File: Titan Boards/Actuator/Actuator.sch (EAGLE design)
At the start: 82 parts, among them Q1 MOSFET-NCH-AO3404A, Q12 MOSFET-NCH-AO3404A, Q13 MOSFET-NCH-AO3404A, Q14 MOSFET-NCH-AO3404A, Q15 MOSFET-NCH-AO3404A, Q17 MOSFET-NCH-AO3404A, Q18 FDD4141TO252, Q2 MOSFET-NCH-AO3404A, Q3 MOSFET-NCH-AO3404A, Q4 MOSFET-NCH-AO3404A, Q5 MOSFET-NCH-AO3404A, Q6 FDD4141TO252, Y1 16MHz, Y3 32.768kHz

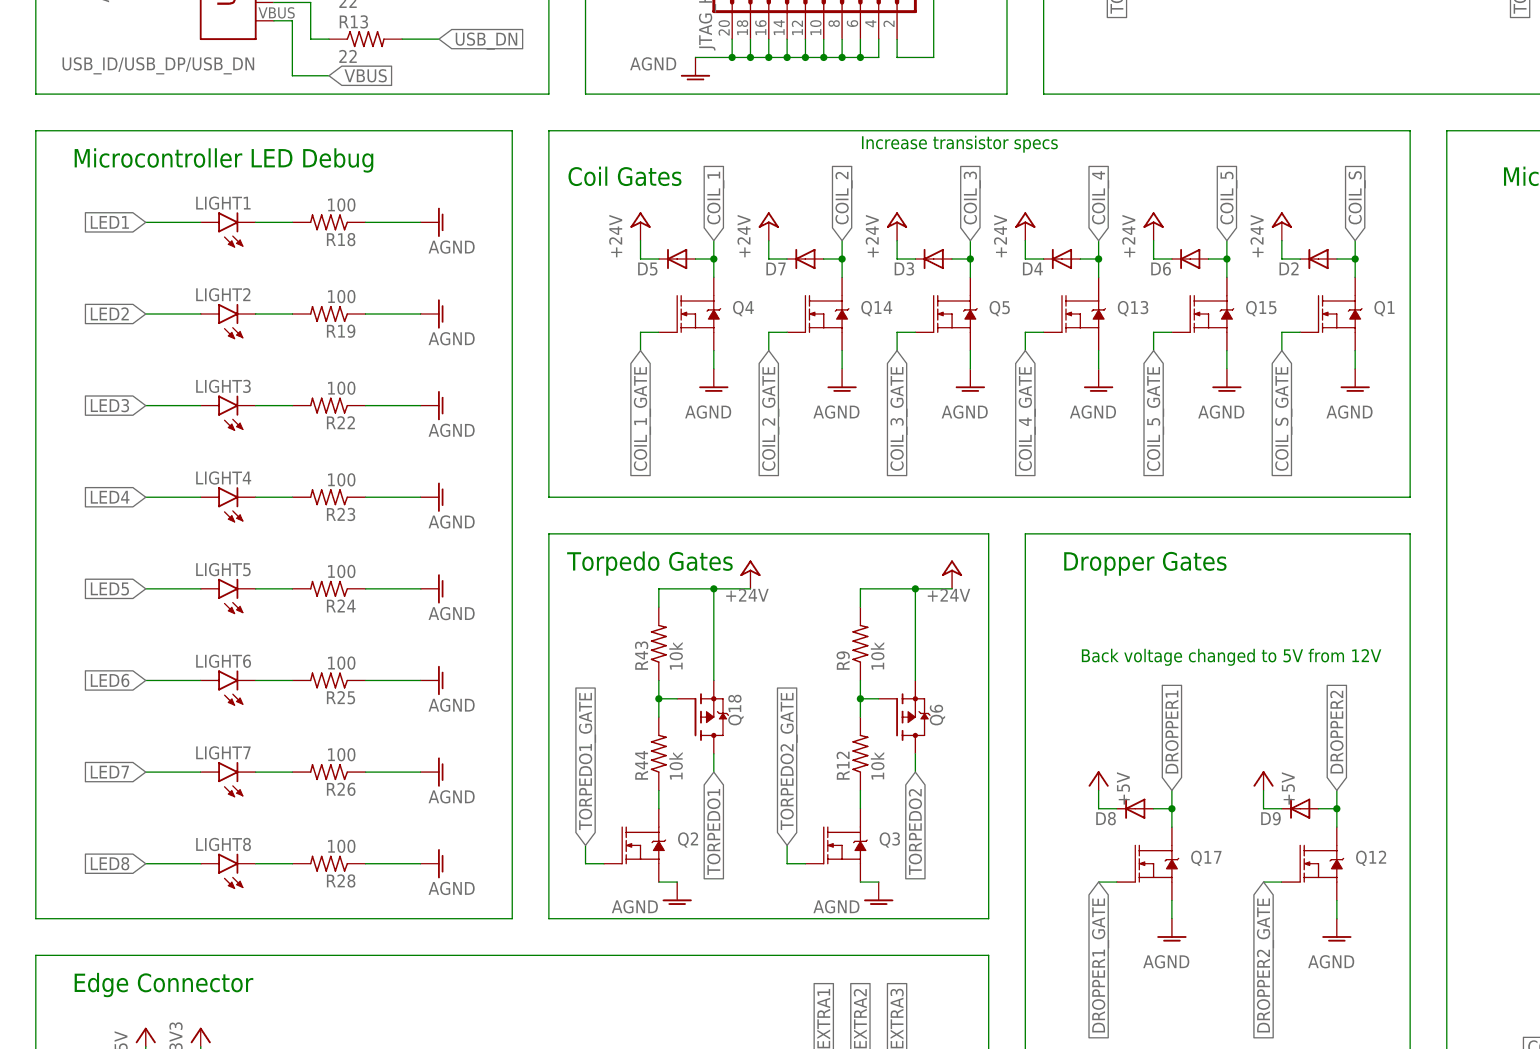
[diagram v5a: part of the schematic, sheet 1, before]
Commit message: Actuator double MOSFET addition
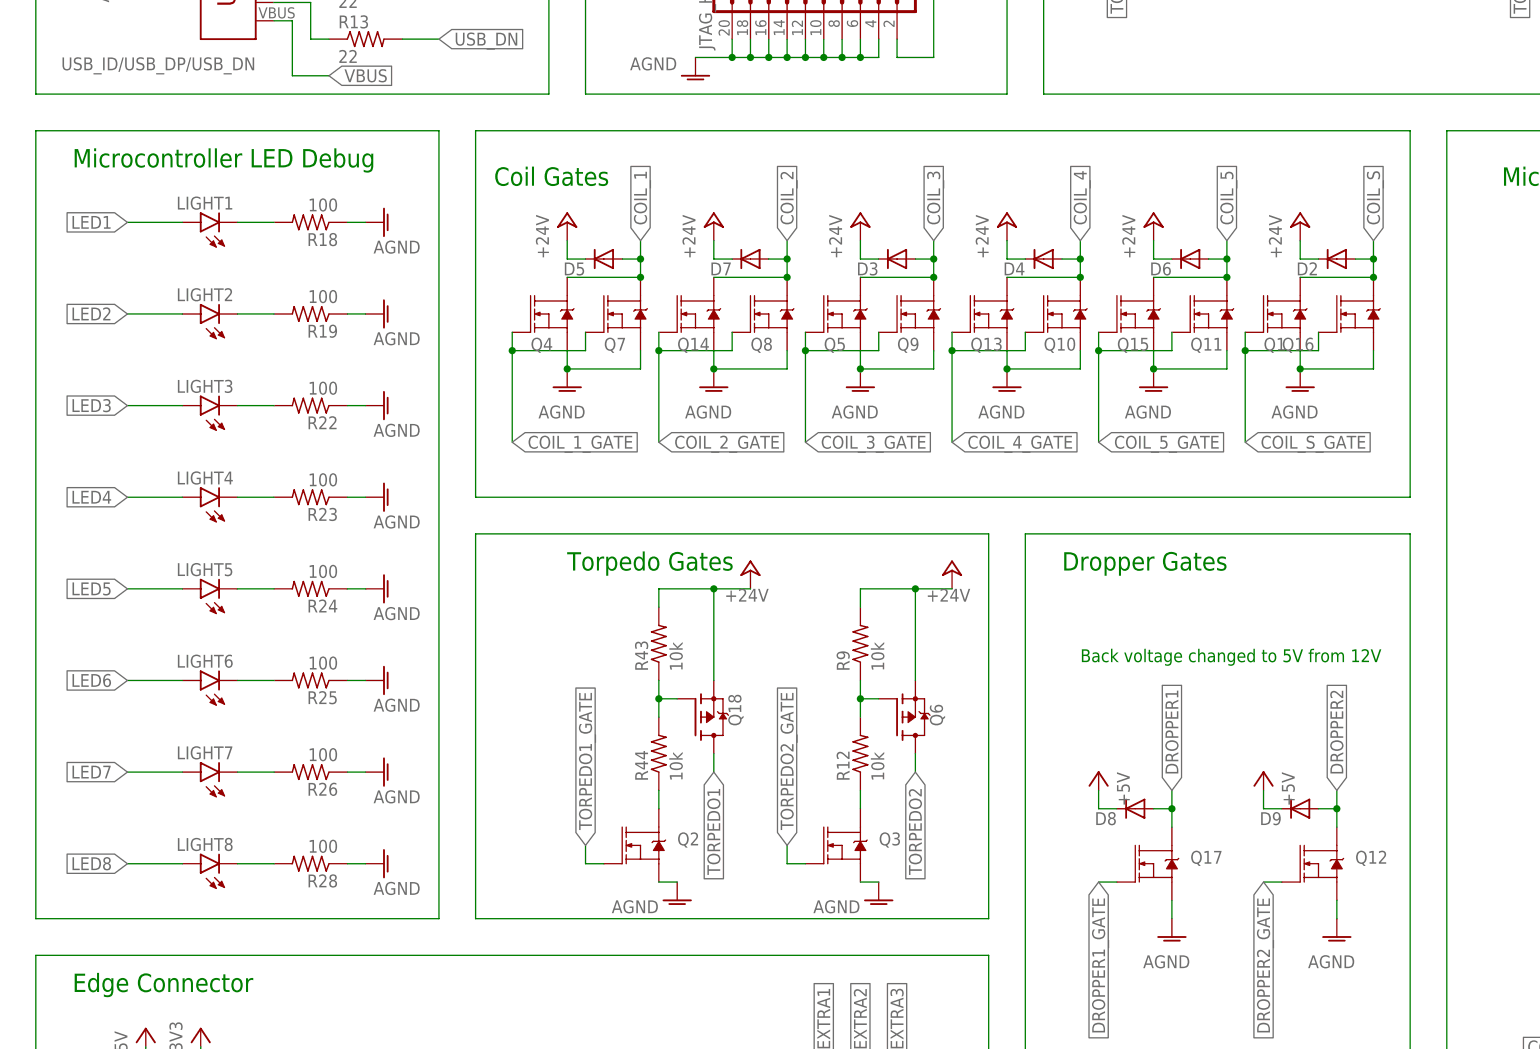
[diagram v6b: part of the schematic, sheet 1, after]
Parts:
- added Q10, Q11, Q16, Q7, Q8, Q9: MOSFET-NCH-AO3404A, SparkFun-DiscreteSemi:MOSFET-NCH-AO3404A
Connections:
- removed net AGND1: Q15.S
- net AGND: now also Q10.S, Q11.S, Q15.S, Q16.S, Q7.S, Q8.S, Q9.S
- net COIL_1: now also Q7.D
- net COIL_1_GATE: now also Q7.G
- net COIL_2: now also Q8.D
- net COIL_2_GATE: now also Q8.G
- net COIL_3: now also Q9.D
- net COIL_3_GATE: now also Q9.G
- net COIL_4: now also Q10.D
- net COIL_4_GATE: now also Q10.G
- net COIL_5: now also Q11.D
- net COIL_5_GATE: now also Q11.G
- net COIL_S: now also Q16.D
- net COIL_S_GATE: now also Q16.G
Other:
- note removed: "Increase transistor specs"
- moved on the sheet: D2, D3, D4, D5, D7, LIGHT1, LIGHT2, LIGHT3, LIGHT4, LIGHT5, LIGHT6, LIGHT7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

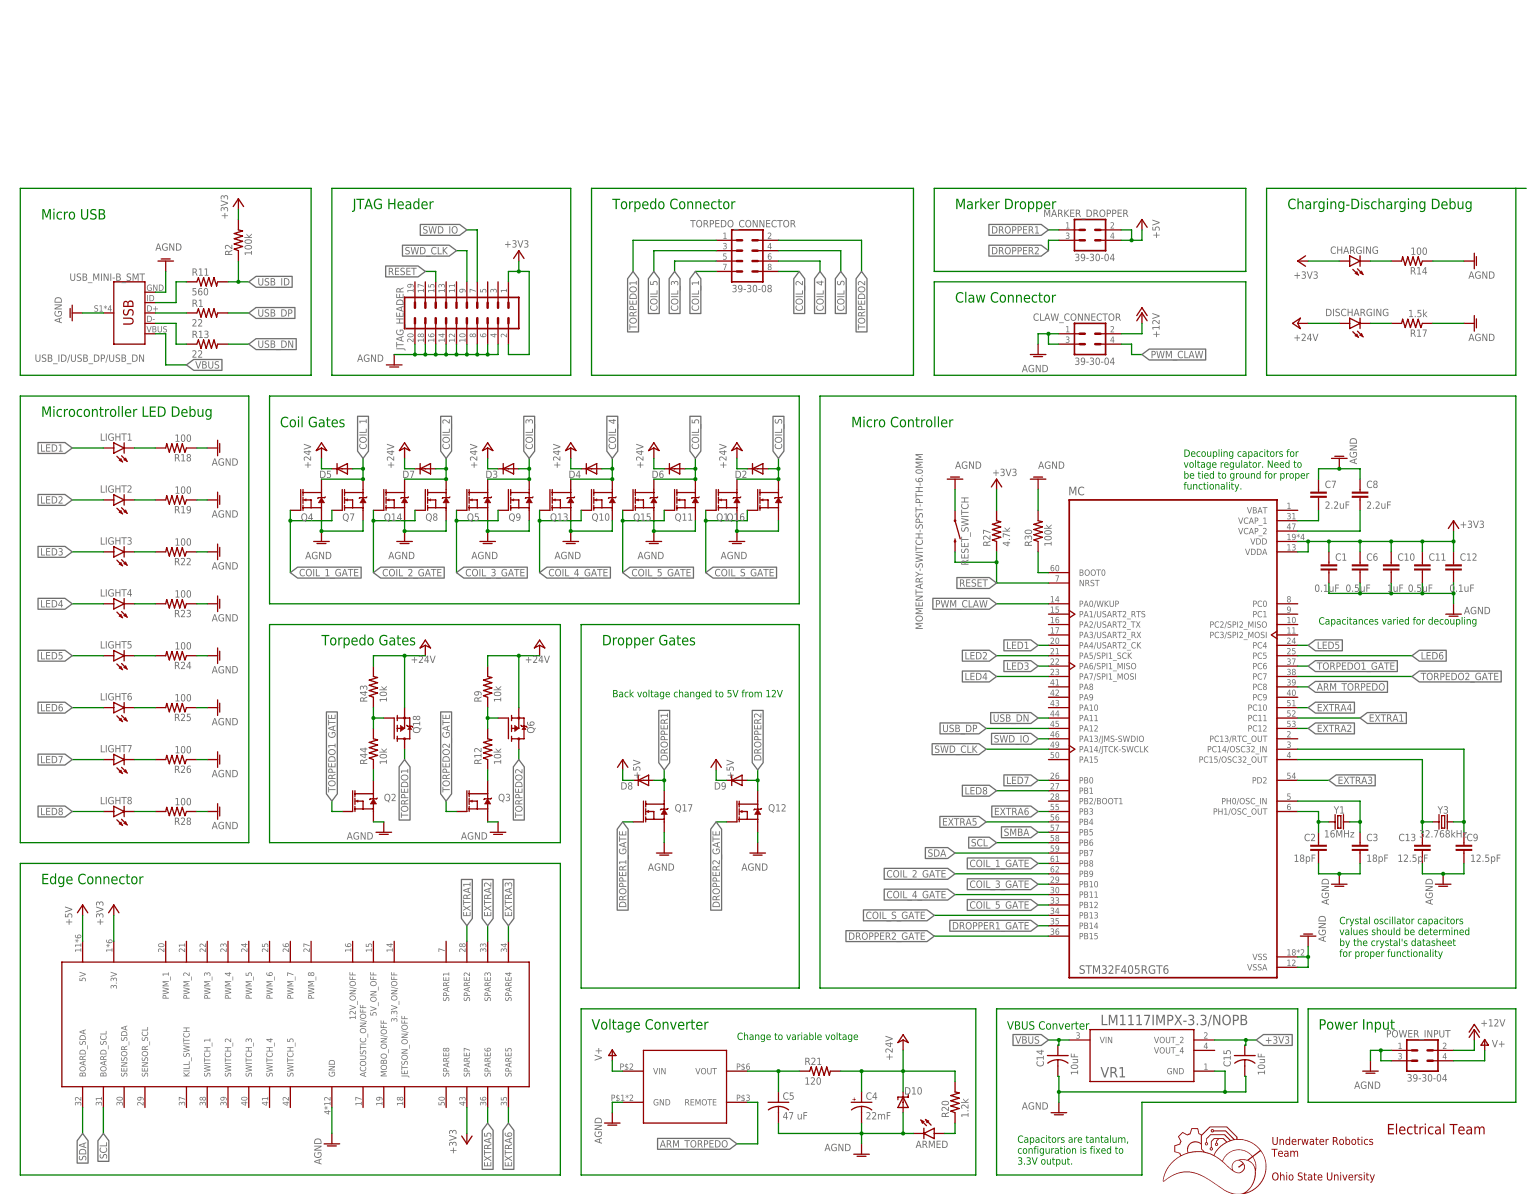
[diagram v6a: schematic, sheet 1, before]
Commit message: Review Actuator changes, varistors
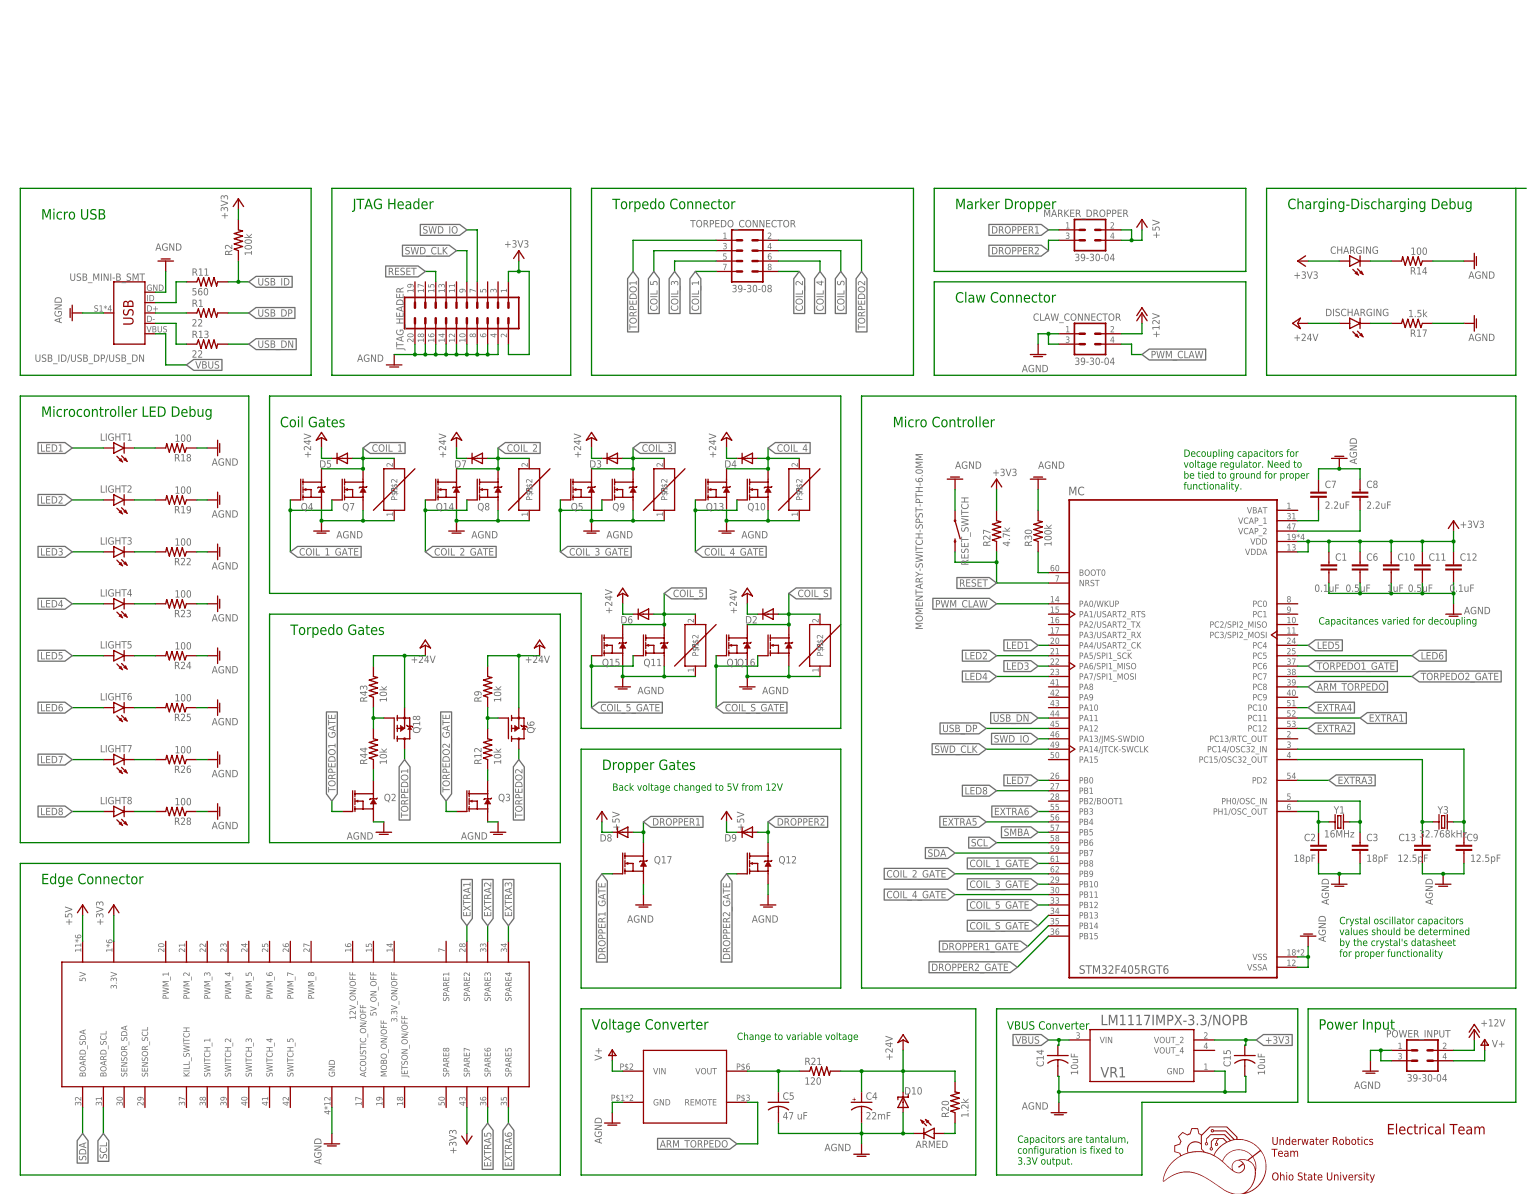
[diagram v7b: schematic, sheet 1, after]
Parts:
- added U$2, U$3, U$4, U$5, U$7, U$8: ERZ-VF2M270ERZ-VF2M270, ERZ-VF2M270:ERZ-VF2M270ERZ-VF2M270
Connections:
- net AGND: now also U$2.P$1, U$3.P$1, U$4.P$1, U$5.P$1, U$7.P$1, U$8.P$1
- net COIL_1: now also U$8.P$2
- net COIL_2: now also U$7.P$2
- net COIL_3: now also U$5.P$2
- net COIL_4: now also U$4.P$2
- net COIL_5: now also U$3.P$2
- net COIL_S: now also U$2.P$2
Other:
- moved on the sheet: D2, D3, D4, D5, D6, D7, D8, D9, Q1, Q10, Q11, Q12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
